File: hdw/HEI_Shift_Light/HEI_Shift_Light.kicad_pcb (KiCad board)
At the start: 2 copper layers, 110 parts, among them J201 VIN, J401 TACH, J501 PICKIT4, J601 USB_C_Receptacle_USB2.0_16P, Q301 DMN3150LW-7, Q302 DMN3150LW-7, Q701 DMN3150LW-7, Q702 DMN3150LW-7, Q703 DMN3150LW-7, U201 TPS26624DRCR, U301 TPS62153, U401 LM2907, U402 MCP4019-103ELT, U501 PIC18F16Q41, U601 FT234XD, U602 ISO7321C

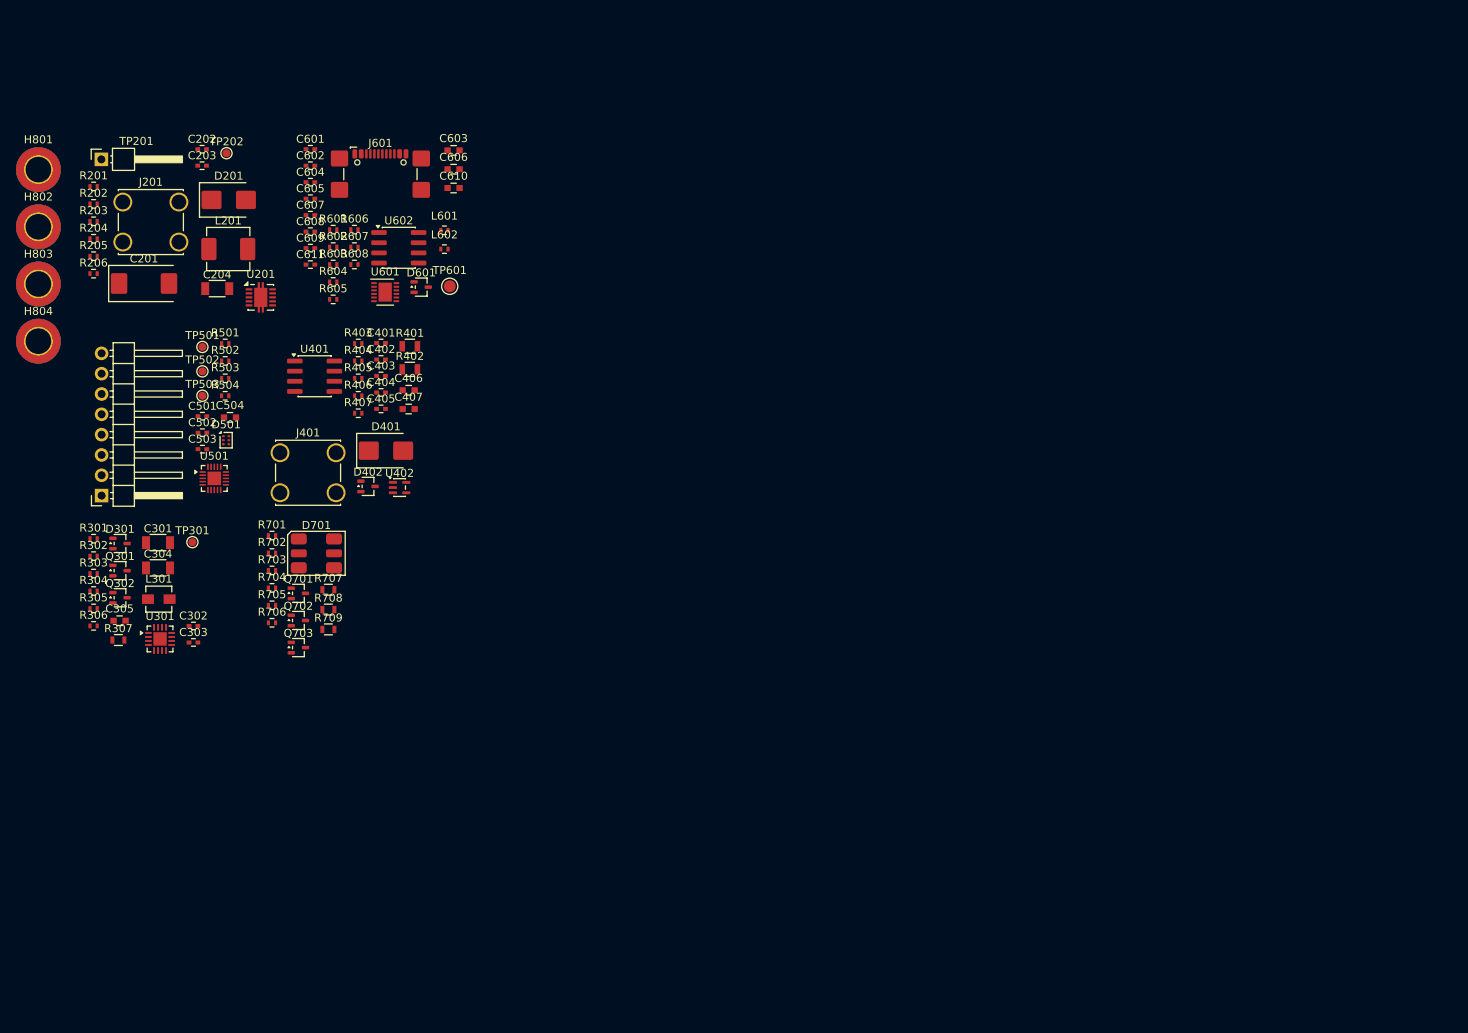
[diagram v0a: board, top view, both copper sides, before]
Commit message: arranged components in PCB
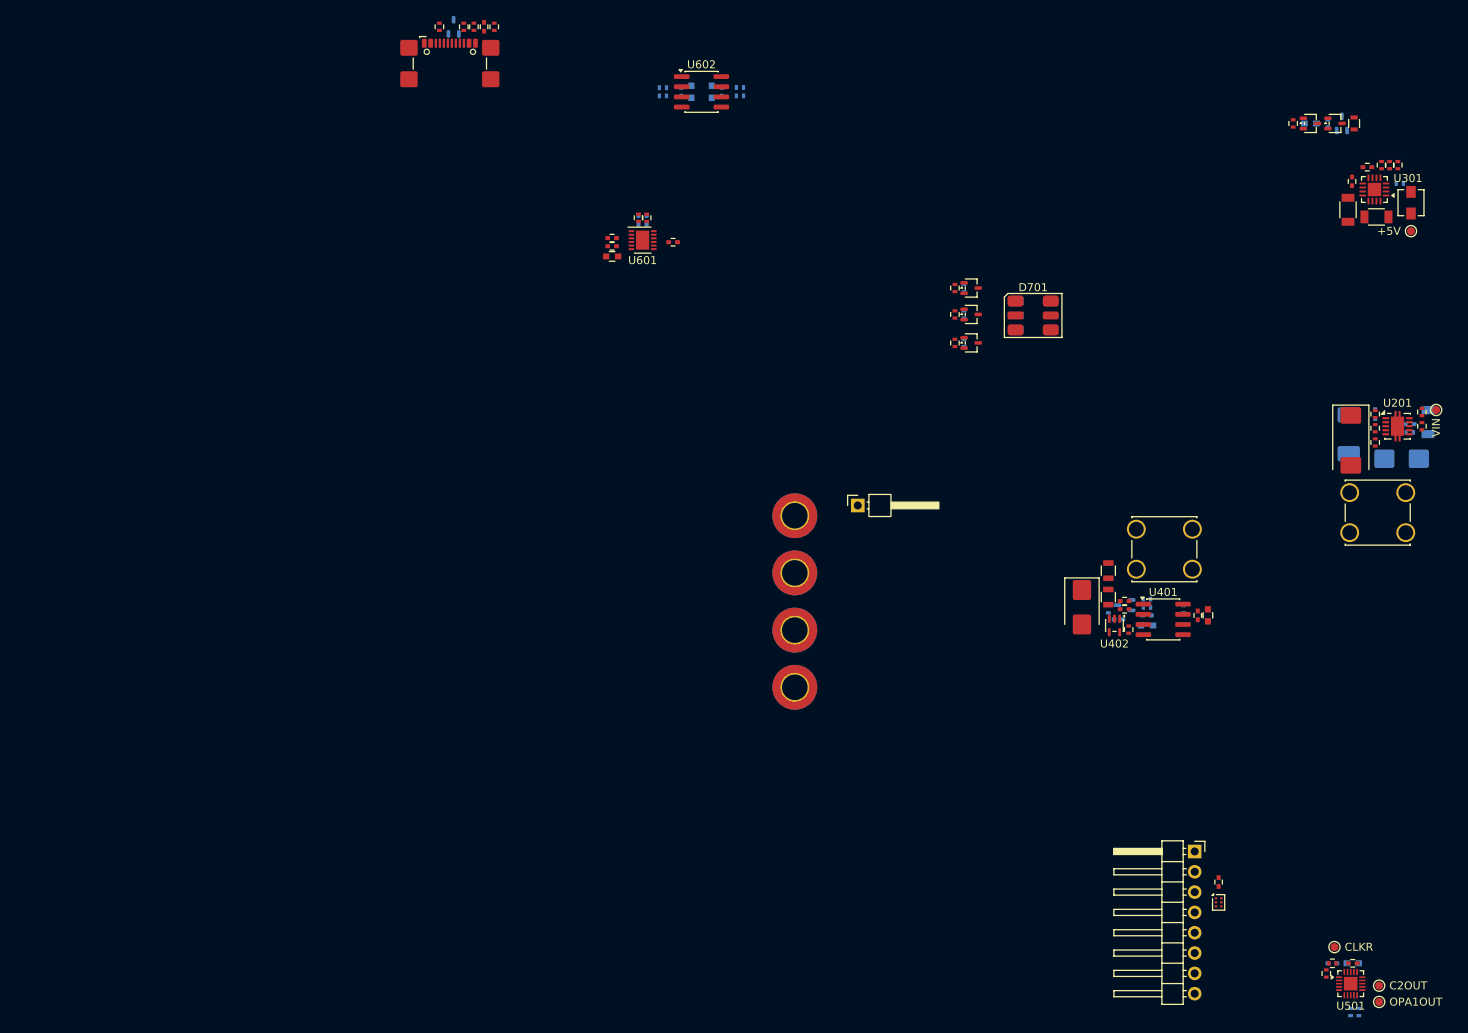
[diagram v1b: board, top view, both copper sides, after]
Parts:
- removed TP601: TP, Custom Footprints Library:Test_Point
- C202, C203, C204, C305, C403, C405, C406, C503, C504, C605, C606, C607, C608, C609, C610, D201, D301, D402, D601, L201, R204, R301, R306, R403, R404, R405, R406, R503, R504, R601, R602, R605, R606, R704, R705, R706, R707, R708, R709: moved to B.Cu
- moved R304 171.5 mm to (230.0, 49.4), turned to -90 degrees
- moved R305 171.2 mm to (229.0, 49.4), turned to 90 degrees
- moved R301 169.2 mm to (230.3, 51.7), turned to 180 degrees
- moved R303 168.9 mm to (228.0, 49.4), turned to 90 degrees
- moved R307 167.4 mm to (224.5, 44.2), turned to -90 degrees
- moved TP501 167.4 mm to (227.7, 152.0)
- moved R205 167.2 mm to (233.0, 80.3), turned to -90 degrees
- moved R206 167.1 mm to (233.0, 82.0), turned to -90 degrees
- moved TP502 166.9 mm to (227.7, 154.0)
- moved R306 166.6 mm to (221.3, 44.2), turned to 90 degrees
- moved R204 166.3 mm to (231.5, 82.8), turned to 180 degrees
- moved L301 164.2 mm to (231.6, 54.1), turned to -90 degrees
- moved Q302 163.0 mm to (222.1, 44.2)
- moved R201 162.7 mm to (227.2, 80.5), turned to -90 degrees
- moved R202 162.6 mm to (227.2, 82.3), turned to -90 degrees
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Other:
- board text added: "+5V"
- board text added: "C2OUT"
- board text added: "CLKR"
- board text added: "OPA1OUT"
- board text added: "VIN"

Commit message: added stackup, design rules
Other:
- copper layers 2 -> 4
- board text added: "JLCPCB JLC04161H-7628"

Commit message: fix some netclass issues
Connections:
- net Net-(D401-Pad1) renamed /Input Signal/TACH_FILT
- net Net-(J201-Pin_1) renamed /Input Power/VIN_BATT
- net Net-(J401-Pin_1) renamed /Input Signal/TACH_IN
- net Net-(U201-IN) renamed /Input Power/VIN_FILT
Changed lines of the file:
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@@
 			(size 0.7 1.3)
 			(layers "F.Cu" "F.Mask" "F.Paste")
-			(net "Net-(J401-Pin_1)")
+			(net "/Input Signal/TACH_IN")
 			(pinfunction "1_1")
 			(pintype "passive")
@@
 			(size 0.7 1.3)
 			(layers "F.Cu" "F.Mask" "F.Paste")
-			(net "Net-(D401-Pad1)")
+			(net "/Input Signal/TACH_FILT")
 			(pinfunction "2_2")
 			(pintype "passive")
@@
 		(sheetname "/Input Signal/")
 		(sheetfile "input_signal.kicad_sch")
+		(units
+			(unit
+				(name "A")
+				(pins "1")
+			)
+		)
 		(attr through_hole)
 		(duplicate_pad_numbers_are_jumpers no)
@@
 			(layers "*.Cu" "*.Mask")
 			(remove_unused_layers no)
-			(net "Net-(J401-Pin_1)")
+			(net "/Input Signal/TACH_IN")
 			(pinfunction "Pin_1_1")
 			(pintype "passive")
@@
 			(layers "*.Cu" "*.Mask")
 			(remove_unused_layers no)
-			(net "Net-(J401-Pin_1)")
+			(net "/Input Signal/TACH_IN")
 			(pinfunction "Pin_1_1")
 			(pintype "passive")
@@
 			(layers "*.Cu" "*.Mask")
 			(remove_unused_layers no)
-			(net "Net-(J401-Pin_1)")
+			(net "/Input Signal/TACH_IN")
 			(pinfunction "Pin_1_1")
 			(pintype "passive")
@@
 			(layers "*.Cu" "*.Mask")
 			(remove_unused_layers no)
-			(net "Net-(J401-Pin_1)")
+			(net "/Input Signal/TACH_IN")
 			(pinfunction "Pin_1_1")
 			(pintype "passive")
@@
 			(size 0.4 0.6)
 			(layers "F.Cu" "F.Mask" "F.Paste")
-			(net "Net-(U201-IN)")
+			(net "/Input Power/VIN_FILT")
 			(pinfunction "1_1")
 			(pintype "passive")
@@
 			(size 0.7 1.3)
 			(layers "F.Cu" "F.Mask" "F.Paste")
-			(net "Net-(D401-Pad1)")
+			(net "/Input Signal/TACH_FILT")
 			(pinfunction "1_1")
 			(pintype "passive")
@@
 			(layers "F.Cu" "F.Mask" "F.Paste")
 			(roundrect_rratio 0.25)
-			(net "Net-(U201-IN)")
+			(net "/Input Power/VIN_FILT")
 			(pinfunction "IN_1")
 			(pintype "power_in")
@@
 		(sheetname "/Input Power/")
 		(sheetfile "input_power.kicad_sch")
+		(units
+			(unit
+				(name "A")
+				(pins "1")
+			)
+		)
 		(attr through_hole)
 		(duplicate_pad_numbers_are_jumpers no)
@@
 			(layers "*.Cu" "*.Mask")
 			(remove_unused_layers no)
-			(net "Net-(J201-Pin_1)")
+			(net "/Input Power/VIN_BATT")
 			(pinfunction "Pin_1_1")
 			(pintype "passive")
@@
 			(layers "*.Cu" "*.Mask")
 			(remove_unused_layers no)
-			(net "Net-(J201-Pin_1)")
+			(net "/Input Power/VIN_BATT")
 			(pinfunction "Pin_1_1")
 			(pintype "passive")
@@
 			(layers "*.Cu" "*.Mask")
 			(remove_unused_layers no)
-			(net "Net-(J201-Pin_1)")
+			(net "/Input Power/VIN_BATT")
 			(pinfunction "Pin_1_1")
 			(pintype "passive")
@@
 			(layers "*.Cu" "*.Mask")
 			(remove_unused_layers no)
-			(net "Net-(J201-Pin_1)")
+			(net "/Input Power/VIN_BATT")
 			(pinfunction "Pin_1_1")
 			(pintype "passive")
@@
 			(layers "F.Cu" "F.Mask" "F.Paste")
 			(roundrect_rratio 0.120773)
-			(net "Net-(U201-IN)")
+			(net "/Input Power/VIN_FILT")
 			(pintype "passive")
 		)
@@
 			(layers "F.Cu" "F.Mask" "F.Paste")
 			(roundrect_rratio 0.1086956522)
-			(net "Net-(D401-Pad1)")
+			(net "/Input Signal/TACH_FILT")
 			(pintype "passive")
 		)
@@
 			(size 0.6 0.5)
 			(layers "B.Cu" "B.Mask" "B.Paste")
-			(net "Net-(U201-IN)")
+			(net "/Input Power/VIN_FILT")
 			(pintype "passive")
 		)
@@
 			(layers "B.Cu" "B.Mask" "B.Paste")
 			(roundrect_rratio 0.1086956522)
-			(net "Net-(J201-Pin_1)")
+			(net "/Input Power/VIN_BATT")
 			(pintype "passive")
 		)
@@
 			(layers "B.Cu" "B.Mask" "B.Paste")
 			(roundrect_rratio 0.131234)
-			(net "Net-(J201-Pin_1)")
+			(net "/Input Power/VIN_BATT")
 			(pinfunction "1_1")
 			(pintype "passive")
@@
 			(layers "B.Cu" "B.Mask" "B.Paste")
 			(roundrect_rratio 0.131234)
-			(net "Net-(U201-IN)")
+			(net "/Input Power/VIN_FILT")
 			(pinfunction "2_2")
 			(pintype "passive")

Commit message: started rough routing
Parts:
- moved C503 0.57 mm to (221.3, 148.9)
- moved R501 0.57 mm to (221.3, 148.9)
- moved R502 0.51 mm to (221.3, 150.0), turned to 180 degrees
- moved L301 0.10 mm to (231.6, 54.2)
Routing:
- net GND: track 0.00 -> 15.5 mm, vias 0 -> 20
- net +5V: track 0.00 -> 5.31 mm, vias 0 -> 11
- net Vin: track 0.00 -> 3.73 mm, vias 0 -> 2
- net Net-(U301-FB): track 0.00 -> 3.23 mm
- net VIN_PGOOD: track 0.00 -> 3.02 mm
- net Net-(U201-OVP): track 0.00 -> 2.71 mm
- net Net-(U301-SS/TR): track 0.00 -> 2.05 mm
- net Net-(C503-Pad1): track 0.00 -> 1.88 mm, vias 0 -> 1
- net ~{PIC18F_MCLR}: track 0.00 -> 1.71 mm
- net Net-(U201-DVDT): track 0.00 -> 1.45 mm, vias 0 -> 1
- net Net-(U201-UVLO): track 0.00 -> 1.44 mm
- net Net-(U201-ILIM): track 0.00 -> 1.35 mm, vias 0 -> 1
- net POS5_PGOOD: track 0.00 -> 1.28 mm, vias 0 -> 1
- net Net-(U201-PAD): track 0.00 -> 1.06 mm
- net POS5_RUN: track 0.00 -> 0.87 mm, vias 0 -> 1
- added copper zone on F.Cu, net +5V
- added copper zone on F.Cu, net GND
- added copper zone on F.Cu, net Net-(L301-Pad1)
- added copper zone on F.Cu, net Vin

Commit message: added reference photos
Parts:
- C611, J601, L601, L602, R607, R608: moved to B.Cu
- D601: moved to F.Cu
- moved R607 269.0 mm to (345.0, 163.3)
- moved J601 266.7 mm to (343.7, 169.1), turned to 180 degrees
- moved D601 265.9 mm to (343.2, 163.3)
- moved R608 263.7 mm to (342.0, 163.3)
- moved L601 261.5 mm to (340.7, 163.3)
- moved C611 259.3 mm to (339.4, 163.3)
- moved L602 257.1 mm to (338.2, 163.3)
- moved H803 217.0 mm to (371.1, 121.9)
- moved R704 212.8 mm to (367.7, 156.7)
- moved R705 212.8 mm to (367.7, 160.0)
- moved R706 212.8 mm to (367.7, 163.6)
- moved D701 212.8 mm to (376.3, 160.1)
- moved R701 212.8 mm to (366.5, 156.7)
- moved R702 212.8 mm to (366.5, 160.0)
- moved R703 212.8 mm to (366.5, 163.6)
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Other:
- board outline added: 54.8 x 55.7 mm

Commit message: came up with rough component placement
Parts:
- added H813: MountingHole_Pad, MountingHole:MountingHole_3.2mm_M3_DIN965_Pad_TopBottom, F.Cu at (100.0, 109.8)
- C201, C301, C302, C303, C304, C401, C402, C404, C407, C501, C502, D401, D501, J201, J401, J501, L301, R201, R202, R203, R205, R206, R303, R304, R305, R401, R402, R407, R501, R502, TP201, TP202, TP301, TP501, TP502, TP503, U201, U301, U401, U402, U501, U602: moved to B.Cu
- C202, C203, C204, C403, C405, C406, C503, C504, C605, C606, C609, C610, D201, D402, L201, R204, R301, R403, R404, R405, R406, R503, R504, R601, R602, R605, R606: moved to F.Cu
- moved H801 253.0 mm to (99.5, 62.2)
- moved J601 239.8 mm to (111.1, 110.7)
- moved C611 239.8 mm to (106.8, 105.0)
- moved D601 239.8 mm to (110.7, 105.0)
- moved L601 239.8 mm to (108.1, 105.0)
- moved L602 239.8 mm to (105.6, 105.0)
- moved R607 239.8 mm to (112.4, 105.0)
- moved R608 239.8 mm to (109.4, 105.0)
- moved H802 236.6 mm to (144.5, 62.2)
- moved H804 234.3 mm to (122.1, 82.2)
- moved D701 230.4 mm to (155.5, 94.0), turned to 90 degrees
- moved R704 229.1 mm to (146.9, 95.7)
- moved R705 229.1 mm to (146.9, 99.0)
- moved R706 229.1 mm to (146.9, 102.5)
- moved Q701 229.1 mm to (147.8, 95.7)
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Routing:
- added copper zone on B.Cu, net +5V
- added copper zone on B.Cu, net GND
- added copper zone on B.Cu, net Net-(L301-Pad1)
- added copper zone on B.Cu, net Vin
- removed copper zone on F.Cu, net +5V
- removed copper zone on F.Cu, net GND
- removed copper zone on F.Cu, net Net-(L301-Pad1)
- removed copper zone on F.Cu, net Vin
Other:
- board size 54.8 x 55.7 mm -> 70.7 x 56.9 mm
- board text added: "GND"
- board text added: "HEI TACH"
- board text added: "PICKIT4"
- board text added: "Switched +12V"

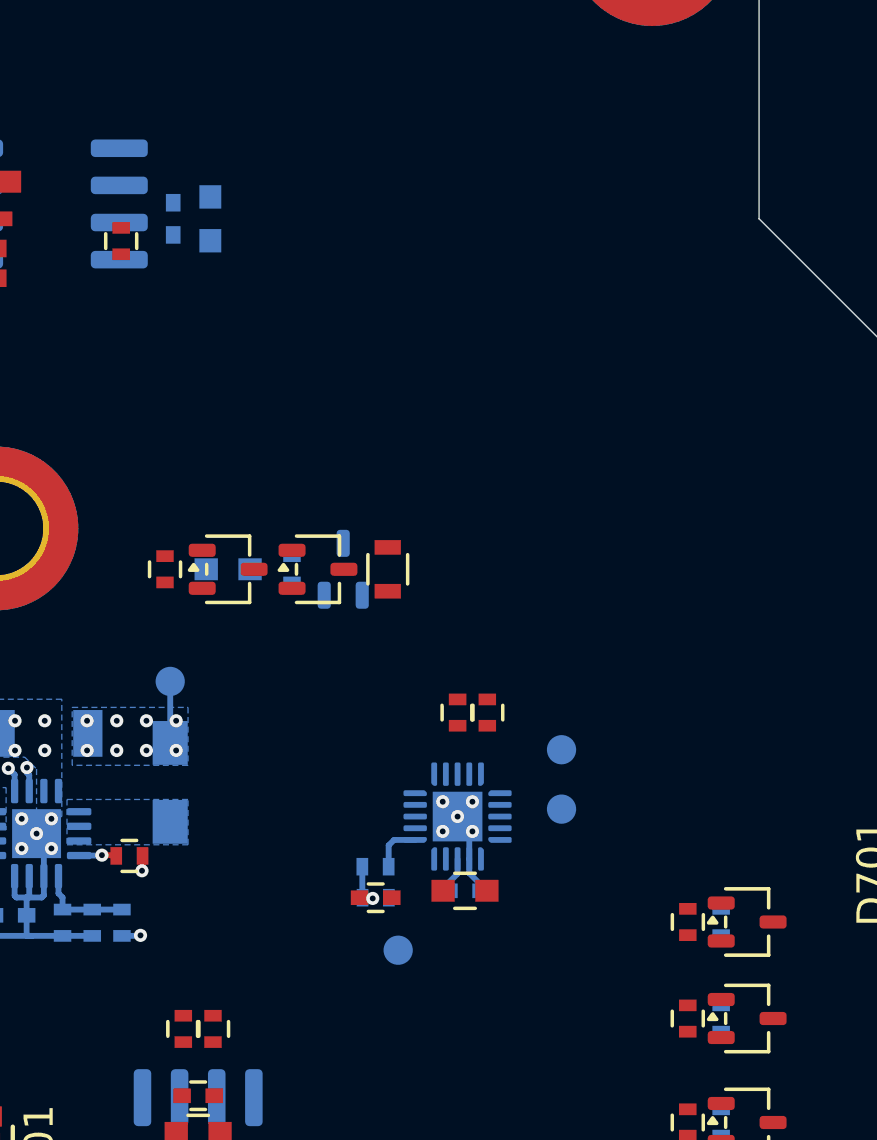
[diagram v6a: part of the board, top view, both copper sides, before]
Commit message: Verified board outline against dash mechanical constraints
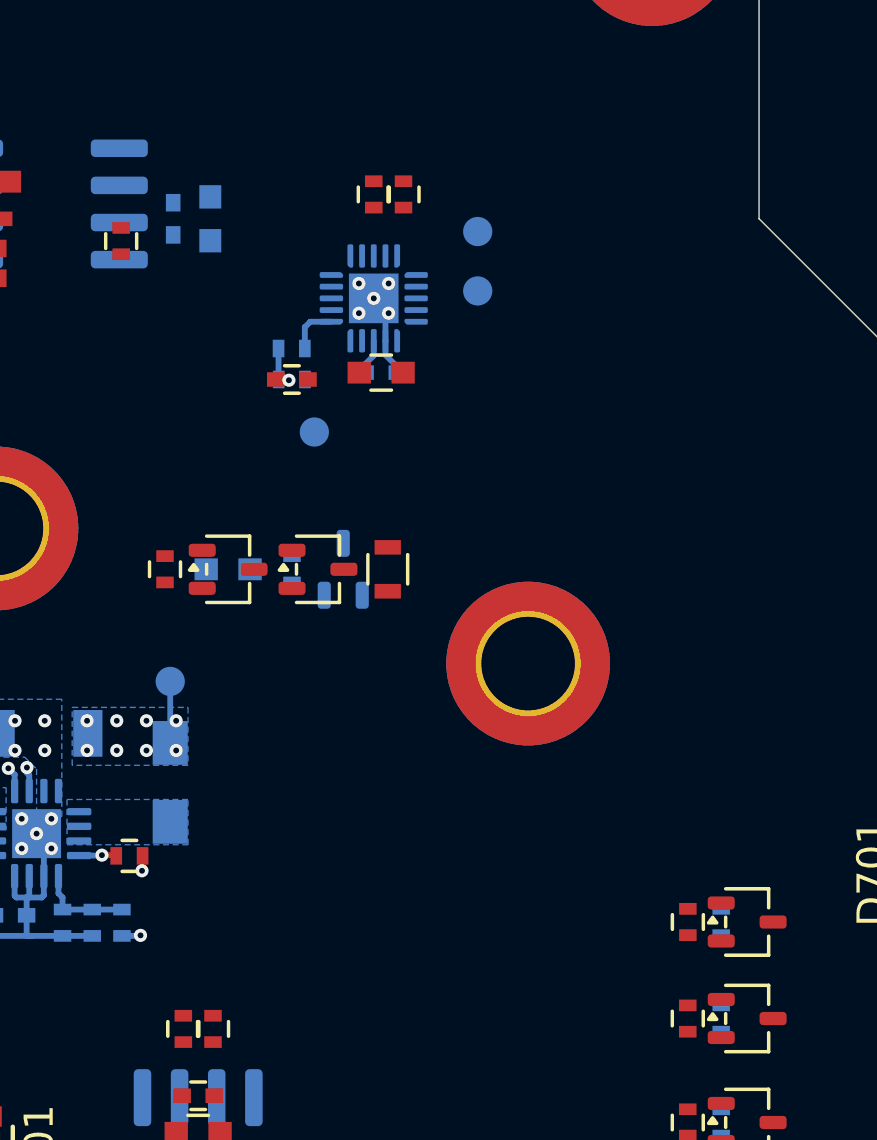
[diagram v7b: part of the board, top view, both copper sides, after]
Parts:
- added H814: MountingHole_Pad, MountingHole:MountingHole_3.2mm_M3_DIN965_Pad_TopBottom, F.Cu at (140.3, 86.8)
- moved C502 18.0 mm to (135.3, 76.9)
- moved C503 18.0 mm to (132.2, 77.1)
- moved C504 18.0 mm to (135.3, 76.9)
- moved R501 18.0 mm to (132.2, 77.1)
- moved R502 18.0 mm to (132.2, 76.1)
- moved R504 18.0 mm to (136.0, 70.8)
- moved TP503 18.0 mm to (133.0, 78.9)
- moved R503 18.0 mm to (135.0, 70.8)
- moved TP501 18.0 mm to (138.6, 74.1)
- moved TP502 18.0 mm to (138.6, 72.1)
- moved U501 18.0 mm to (135.0, 74.3)
